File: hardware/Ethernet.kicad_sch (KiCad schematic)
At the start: 39 parts

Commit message: Assign footprints to some components and improvements.
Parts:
- C? (x16): footprint (none) -> Capacitor_SMD:C_0603_1608Metric_Pad1.08x0.95mm_HandSolder
- FB?: footprint (none) -> Inductor_SMD:L_0603_1608Metric_Pad1.05x0.95mm_HandSolder
- R? (x15): footprint (none) -> Resistor_SMD:R_0805_2012Metric_Pad1.20x1.40mm_HandSolder
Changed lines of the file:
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@@
 			)
 		)
-		(property "Footprint" ""
+		(property "Footprint" "Resistor_SMD:R_0805_2012Metric_Pad1.20x1.40mm_HandSolder"
 			(at 38.862 113.03 90)
 			(effects
@@
 			)
 		)
-		(property "Footprint" ""
+		(property "Footprint" "Resistor_SMD:R_0805_2012Metric_Pad1.20x1.40mm_HandSolder"
 			(at 153.162 138.43 90)
 			(effects
@@
 			)
 		)
-		(property "Footprint" ""
+		(property "Footprint" "Resistor_SMD:R_0805_2012Metric_Pad1.20x1.40mm_HandSolder"
 			(at 163.322 101.6 90)
 			(effects
@@
 			)
 		)
-		(property "Footprint" ""
+		(property "Footprint" "Resistor_SMD:R_0805_2012Metric_Pad1.20x1.40mm_HandSolder"
 			(at 73.152 116.84 90)
 			(effects
@@
 			)
 		)
-		(property "Footprint" ""
+		(property "Footprint" "Resistor_SMD:R_0805_2012Metric_Pad1.20x1.40mm_HandSolder"
 			(at 97.79 117.348 90)
 			(effects
@@
 			)
 		)
-		(property "Footprint" ""
+		(property "Footprint" "Capacitor_SMD:C_0603_1608Metric_Pad1.08x0.95mm_HandSolder"
 			(at 55.5752 82.55 0)
 			(effects
@@
 			)
 		)
-		(property "Footprint" ""
+		(property "Footprint" "Capacitor_SMD:C_0603_1608Metric_Pad1.08x0.95mm_HandSolder"
 			(at 188.9252 129.54 0)
 			(effects
@@
 			)
 		)
-		(property "Footprint" ""
+		(property "Footprint" "Resistor_SMD:R_0805_2012Metric_Pad1.20x1.40mm_HandSolder"
 			(at 51.562 149.86 90)
 			(effects
@@
 			)
 		)
-		(property "Footprint" ""
+		(property "Footprint" "Capacitor_SMD:C_0603_1608Metric_Pad1.08x0.95mm_HandSolder"
 			(at 141.9352 45.72 0)
 			(effects
@@
 			)
 		)
-		(property "Footprint" ""
+		(property "Footprint" "Capacitor_SMD:C_0603_1608Metric_Pad1.08x0.95mm_HandSolder"
 			(at 96.2152 154.94 0)
 			(effects
@@
 			)
 		)
-		(property "Footprint" ""
+		(property "Footprint" "Resistor_SMD:R_0805_2012Metric_Pad1.20x1.40mm_HandSolder"
 			(at 60.452 116.84 90)
 			(effects
@@
 			)
 		)
-		(property "Footprint" ""
+		(property "Footprint" "Capacitor_SMD:C_0603_1608Metric_Pad1.08x0.95mm_HandSolder"
 			(at 108.9152 45.72 0)
 			(effects
@@
 			)
 		)
-		(property "Footprint" ""
+		(property "Footprint" "Capacitor_SMD:C_0603_1608Metric_Pad1.08x0.95mm_HandSolder"
 			(at 79.7052 154.94 0)
 			(effects
@@
 			)
 		)
-		(property "Footprint" ""
+		(property "Footprint" "Inductor_SMD:L_0603_1608Metric_Pad1.05x0.95mm_HandSolder"
 			(at 118.11 34.798 90)
 			(effects
@@
 			)
 		)
-		(property "Footprint" ""
+		(property "Footprint" "Capacitor_SMD:C_0603_1608Metric_Pad1.08x0.95mm_HandSolder"
 			(at 135.5852 78.74 0)
 			(effects
@@
 			)
 		)
-		(property "Footprint" ""
+		(property "Footprint" "Resistor_SMD:R_0805_2012Metric_Pad1.20x1.40mm_HandSolder"
 			(at 155.702 101.6 90)
 			(effects
@@
 			)
 		)
-		(property "Footprint" ""
+		(property "Footprint" "Resistor_SMD:R_0805_2012Metric_Pad1.20x1.40mm_HandSolder"
 			(at 261.62 108.458 90)
 			(effects
@@
 			)
 		)
-		(property "Footprint" ""
+		(property "Footprint" "Capacitor_SMD:C_0603_1608Metric_Pad1.08x0.95mm_HandSolder"
 			(at 68.2752 82.55 0)
 			(effects
@@
 			)
 		)
-		(property "Footprint" ""
+		(property "Footprint" "Capacitor_SMD:C_0603_1608Metric_Pad1.08x0.95mm_HandSolder"
 			(at 96.2152 45.72 0)
 			(effects
@@
 			)
 		)
-		(property "Footprint" ""
+		(property "Footprint" "Resistor_SMD:R_0805_2012Metric_Pad1.20x1.40mm_HandSolder"
 			(at 170.942 101.6 90)
 			(effects
@@
 			)
 		)
-		(property "Footprint" ""
+		(property "Footprint" "Capacitor_SMD:C_0603_1608Metric_Pad1.08x0.95mm_HandSolder"
 			(at 152.0952 78.74 0)
 			(effects
@@
 			)
 		)
-		(property "Footprint" ""
+		(property "Footprint" "Resistor_SMD:R_0805_2012Metric_Pad1.20x1.40mm_HandSolder"
 			(at 97.79 114.808 90)
 			(effects
@@
 			)
 		)
-		(property "Footprint" ""
+		(property "Footprint" "Resistor_SMD:R_0805_2012Metric_Pad1.20x1.40mm_HandSolder"
 			(at 261.62 118.618 90)
 			(effects
@@
 			)
 		)
-		(property "Footprint" ""
+		(property "Footprint" "Capacitor_SMD:C_0603_1608Metric_Pad1.08x0.95mm_HandSolder"
 			(at 103.8352 78.74 0)
 			(effects
@@
 			)
 		)
-		(property "Footprint" ""
+		(property "Footprint" "Resistor_SMD:R_0805_2012Metric_Pad1.20x1.40mm_HandSolder"
 			(at 44.45 135.128 90)
 			(effects
@@
 			)
 		)
-		(property "Footprint" ""
+		(property "Footprint" "Capacitor_SMD:C_0603_1608Metric_Pad1.08x0.95mm_HandSolder"
 			(at 129.2352 45.72 0)
 			(effects
@@
 			)
 		)
-		(property "Footprint" ""
+		(property "Footprint" "Resistor_SMD:R_0805_2012Metric_Pad1.20x1.40mm_HandSolder"
 			(at 97.79 122.428 90)
 			(effects
@@
 			)
 		)
-		(property "Footprint" ""
+		(property "Footprint" "Capacitor_SMD:C_0603_1608Metric_Pad1.08x0.95mm_HandSolder"
 			(at 79.7052 82.55 0)
 			(effects
@@
 			)
 		)
-		(property "Footprint" ""
+		(property "Footprint" "Capacitor_SMD:C_0603_1608Metric_Pad1.08x0.95mm_HandSolder"
 			(at 154.6352 45.72 0)
 			(effects
@@
 			)
 		)
-		(property "Footprint" ""
+		(property "Footprint" "Capacitor_SMD:C_0603_1608Metric_Pad1.08x0.95mm_HandSolder"
 			(at 83.5152 45.72 0)
 			(effects
@@
 			)
 		)
-		(property "Footprint" ""
+		(property "Footprint" "Capacitor_SMD:C_0603_1608Metric_Pad1.08x0.95mm_HandSolder"
 			(at 113.9952 78.74 0)
 			(effects
@@
 			)
 		)
-		(property "Footprint" ""
+		(property "Footprint" "Resistor_SMD:R_0805_2012Metric_Pad1.20x1.40mm_HandSolder"
 			(at 178.562 101.6 90)
 			(effects

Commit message: Improvements to schematic.
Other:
- company: (none) -> FEYTECH PTY LTD
- title: (none) -> MQTT Gateway
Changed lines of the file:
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@@
 	(generator_version "9.0")
 	(paper "A4")
+	(title_block
+		(title "MQTT Gateway")
+		(date "2026-03-13")
+		(rev "V1.0.0")
+		(company "FEYTECH PTY LTD")
+	)
 	(junction
 		(at 62.23 105.41)

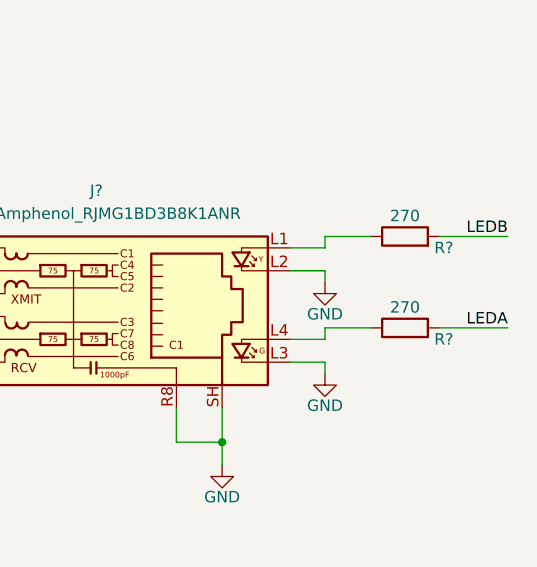
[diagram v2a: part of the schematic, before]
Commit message: Add footprint to components
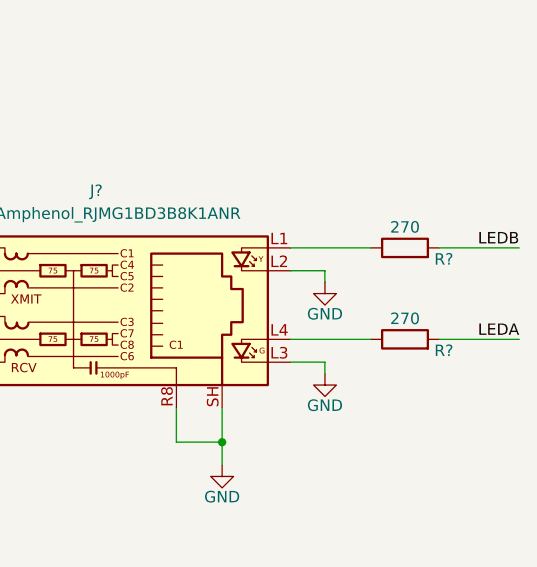
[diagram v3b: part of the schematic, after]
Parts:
- R? (x15): footprint Resistor_SMD:R_0805_2012Metric_Pad1.20x1.40mm_HandSolder -> Resistor_SMD:R_0603_1608Metric_Pad0.98x0.95mm_HandSolder
- R?: footprint (none) -> Resistor_SMD:R_0603_1608Metric_Pad0.98x0.95mm_HandSolder
- TP? (x2): footprint (none) -> TestPoint:TestPoint_Pad_D1.0mm
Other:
- moved on the sheet: R?
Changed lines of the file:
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@@
 	(wire
 		(pts
-			(xy 252.73 106.68) (xy 257.81 106.68)
-		)
-		(stroke
-			(width 0)
-			(type default)
-		)
-	)
-	(wire
-		(pts
 			(xy 153.67 33.02) (xy 153.67 38.1)
 		)
@@
 	(wire
 		(pts
-			(xy 265.43 116.84) (xy 273.05 116.84)
+			(xy 265.43 118.11) (xy 274.32 118.11)
 		)
 		(stroke
@@
 	(wire
 		(pts
-			(xy 252.73 118.11) (xy 252.73 116.84)
-		)
-		(stroke
-			(width 0)
-			(type default)
-		)
-	)
-	(wire
-		(pts
 			(xy 29.21 105.41) (xy 40.64 105.41)
 		)
@@
 	(wire
 		(pts
-			(xy 248.92 118.11) (xy 252.73 118.11)
+			(xy 248.92 118.11) (xy 257.81 118.11)
 		)
 		(stroke
@@
 	(wire
 		(pts
-			(xy 252.73 107.95) (xy 252.73 106.68)
-		)
-		(stroke
-			(width 0)
-			(type default)
-		)
-	)
-	(wire
-		(pts
 			(xy 113.03 69.85) (xy 102.87 69.85)
 		)
@@
 	(wire
 		(pts
-			(xy 252.73 116.84) (xy 257.81 116.84)
-		)
-		(stroke
-			(width 0)
-			(type default)
-		)
-	)
-	(wire
-		(pts
 			(xy 86.36 151.13) (xy 86.36 156.21)
 		)
@@
 	(wire
 		(pts
-			(xy 248.92 107.95) (xy 252.73 107.95)
+			(xy 248.92 107.95) (xy 257.81 107.95)
 		)
 		(stroke
@@
 	(wire
 		(pts
-			(xy 265.43 106.68) (xy 273.05 106.68)
+			(xy 265.43 107.95) (xy 274.32 107.95)
 		)
 		(stroke
@@
 	)
 	(label "LEDB"
-		(at 273.05 106.68 180)
+		(at 274.32 107.95 180)
 		(effects
 			(font
@@
 	)
 	(label "LEDA"
-		(at 273.05 116.84 180)
+		(at 274.32 118.11 180)
 		(effects
 			(font
@@
 			)
 		)
-		(property "Footprint" "Resistor_SMD:R_0805_2012Metric_Pad1.20x1.40mm_HandSolder"
+		(property "Footprint" "Resistor_SMD:R_0603_1608Metric_Pad0.98x0.95mm_HandSolder"
 			(at 38.862 113.03 90)
 			(effects
@@
 			)
 		)
-		(property "Footprint" "Resistor_SMD:R_0805_2012Metric_Pad1.20x1.40mm_HandSolder"
+		(property "Footprint" "Resistor_SMD:R_0603_1608Metric_Pad0.98x0.95mm_HandSolder"
 			(at 153.162 138.43 90)
 			(effects
@@
 			)
 		)
-		(property "Footprint" "Resistor_SMD:R_0805_2012Metric_Pad1.20x1.40mm_HandSolder"
+		(property "Footprint" "Resistor_SMD:R_0603_1608Metric_Pad0.98x0.95mm_HandSolder"
 			(at 163.322 101.6 90)
 			(effects
@@
 			)
 		)
-		(property "Footprint" "Resistor_SMD:R_0805_2012Metric_Pad1.20x1.40mm_HandSolder"
+		(property "Footprint" "Resistor_SMD:R_0603_1608Metric_Pad0.98x0.95mm_HandSolder"
 			(at 73.152 116.84 90)
 			(effects
@@
 			)
 		)
-		(property "Footprint" "Resistor_SMD:R_0805_2012Metric_Pad1.20x1.40mm_HandSolder"
+		(property "Footprint" "Resistor_SMD:R_0603_1608Metric_Pad0.98x0.95mm_HandSolder"
 			(at 97.79 117.348 90)
 			(effects
@@
 			)
 		)
-		(property "Footprint" "Resistor_SMD:R_0805_2012Metric_Pad1.20x1.40mm_HandSolder"
+		(property "Footprint" "Resistor_SMD:R_0603_1608Metric_Pad0.98x0.95mm_HandSolder"
 			(at 51.562 149.86 90)
 			(effects
@@
 			)
 		)
-		(property "Footprint" "Resistor_SMD:R_0805_2012Metric_Pad1.20x1.40mm_HandSolder"
+		(property "Footprint" "Resistor_SMD:R_0603_1608Metric_Pad0.98x0.95mm_HandSolder"
 			(at 60.452 116.84 90)
 			(effects
@@
 			)
 		)
-		(property "Footprint" ""
+		(property "Footprint" "TestPoint:TestPoint_Pad_D1.0mm"
 			(at 133.35 33.02 0)
 			(effects
@@
 			)
 		)
-		(property "Footprint" ""
+		(property "Footprint" "Resistor_SMD:R_0603_1608Metric_Pad0.98x0.95mm_HandSolder"
 			(at 47.752 116.84 90)
 			(effects
@@
 			)
 		)
-		(property "Footprint" "Resistor_SMD:R_0805_2012Metric_Pad1.20x1.40mm_HandSolder"
+		(property "Footprint" "Resistor_SMD:R_0603_1608Metric_Pad0.98x0.95mm_HandSolder"
 			(at 155.702 101.6 90)
 			(effects
@@
 	(symbol
 		(lib_id "Device:R")
-		(at 261.62 106.68 90)
+		(at 261.62 107.95 90)
 		(unit 1)
 		(exclude_from_sim no)
@@
 		(dnp no)
 		(property "Reference" "R?"
-			(at 265.938 107.95 90)
+			(at 265.938 109.22 90)
 			(effects
 				(font
@@
 		)
 		(property "Value" "270"
-			(at 261.62 104.394 90)
+			(at 261.62 105.664 90)
 			(effects
 				(font
@@
 			)
 		)
-		(property "Footprint" "Resistor_SMD:R_0805_2012Metric_Pad1.20x1.40mm_HandSolder"
-			(at 261.62 108.458 90)
+		(property "Footprint" "Resistor_SMD:R_0603_1608Metric_Pad0.98x0.95mm_HandSolder"
+			(at 261.62 109.728 90)
 			(effects
 				(font
@@
 		)
 		(property "Datasheet" "~"
-			(at 261.62 106.68 0)
+			(at 261.62 107.95 0)
 			(effects
 				(font
@@
 		)
 		(property "Description" "Resistor"
-			(at 261.62 106.68 0)
+			(at 261.62 107.95 0)
 			(effects
 				(font
@@
 			)
 		)
-		(property "Footprint" "Resistor_SMD:R_0805_2012Metric_Pad1.20x1.40mm_HandSolder"
+		(property "Footprint" "Resistor_SMD:R_0603_1608Metric_Pad0.98x0.95mm_HandSolder"
 			(at 170.942 101.6 90)
 			(effects
@@
 			)
 		)
-		(property "Footprint" "Resistor_SMD:R_0805_2012Metric_Pad1.20x1.40mm_HandSolder"
+		(property "Footprint" "Resistor_SMD:R_0603_1608Metric_Pad0.98x0.95mm_HandSolder"
 			(at 97.79 114.808 90)
 			(effects
@@
 	(symbol
 		(lib_id "Device:R")
-		(at 261.62 116.84 90)
+		(at 261.62 118.11 90)
 		(unit 1)
 		(exclude_from_sim no)
@@
 		(dnp no)
 		(property "Reference" "R?"
-			(at 265.938 118.11 90)
+			(at 265.938 119.38 90)
 			(effects
 				(font
@@
 		)
 		(property "Value" "270"
-			(at 261.62 114.554 90)
+			(at 261.62 115.824 90)
 			(effects
 				(font
@@
 			)
 		)
-		(property "Footprint" "Resistor_SMD:R_0805_2012Metric_Pad1.20x1.40mm_HandSolder"
-			(at 261.62 118.618 90)
+		(property "Footprint" "Resistor_SMD:R_0603_1608Metric_Pad0.98x0.95mm_HandSolder"
+			(at 261.62 119.888 90)
 			(effects
 				(font
@@
 		)
 		(property "Datasheet" "~"
-			(at 261.62 116.84 0)
+			(at 261.62 118.11 0)
 			(effects
 				(font
@@
 		)
 		(property "Description" "Resistor"
-			(at 261.62 116.84 0)
+			(at 261.62 118.11 0)
 			(effects
 				(font
@@
 			)
 		)
-		(property "Footprint" "Resistor_SMD:R_0805_2012Metric_Pad1.20x1.40mm_HandSolder"
+		(property "Footprint" "Resistor_SMD:R_0603_1608Metric_Pad0.98x0.95mm_HandSolder"
 			(at 44.45 135.128 90)
 			(effects
@@
 			)
 		)
-		(property "Footprint" "Resistor_SMD:R_0805_2012Metric_Pad1.20x1.40mm_HandSolder"
+		(property "Footprint" "Resistor_SMD:R_0603_1608Metric_Pad0.98x0.95mm_HandSolder"
 			(at 97.79 122.428 90)
 			(effects
@@
 			)
 		)
-		(property "Footprint" ""
+		(property "Footprint" "TestPoint:TestPoint_Pad_D1.0mm"
 			(at 113.03 33.02 0)
 			(effects
@@
 			)
 		)
-		(property "Footprint" "Resistor_SMD:R_0805_2012Metric_Pad1.20x1.40mm_HandSolder"
+		(property "Footprint" "Resistor_SMD:R_0603_1608Metric_Pad0.98x0.95mm_HandSolder"
 			(at 178.562 101.6 90)
 			(effects

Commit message: Improvements
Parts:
- Y3: renamed from Y?; footprint (none) -> Crystal:Crystal_SMD_3225-4Pin_3.2x2.5mm
- gave numbers to parts that had none: 38
